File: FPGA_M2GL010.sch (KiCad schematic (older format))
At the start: 19 parts

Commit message: Does this actually work, Git?
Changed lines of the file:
@@
 Text Notes 5750 2700 0    50   ~ 10
 2.5V BANK!!
+Wire Wire Line
+	6150 5950 6150 6000
+Wire Wire Line
+	5550 5950 6150 5950
 $EndSCHEMATC

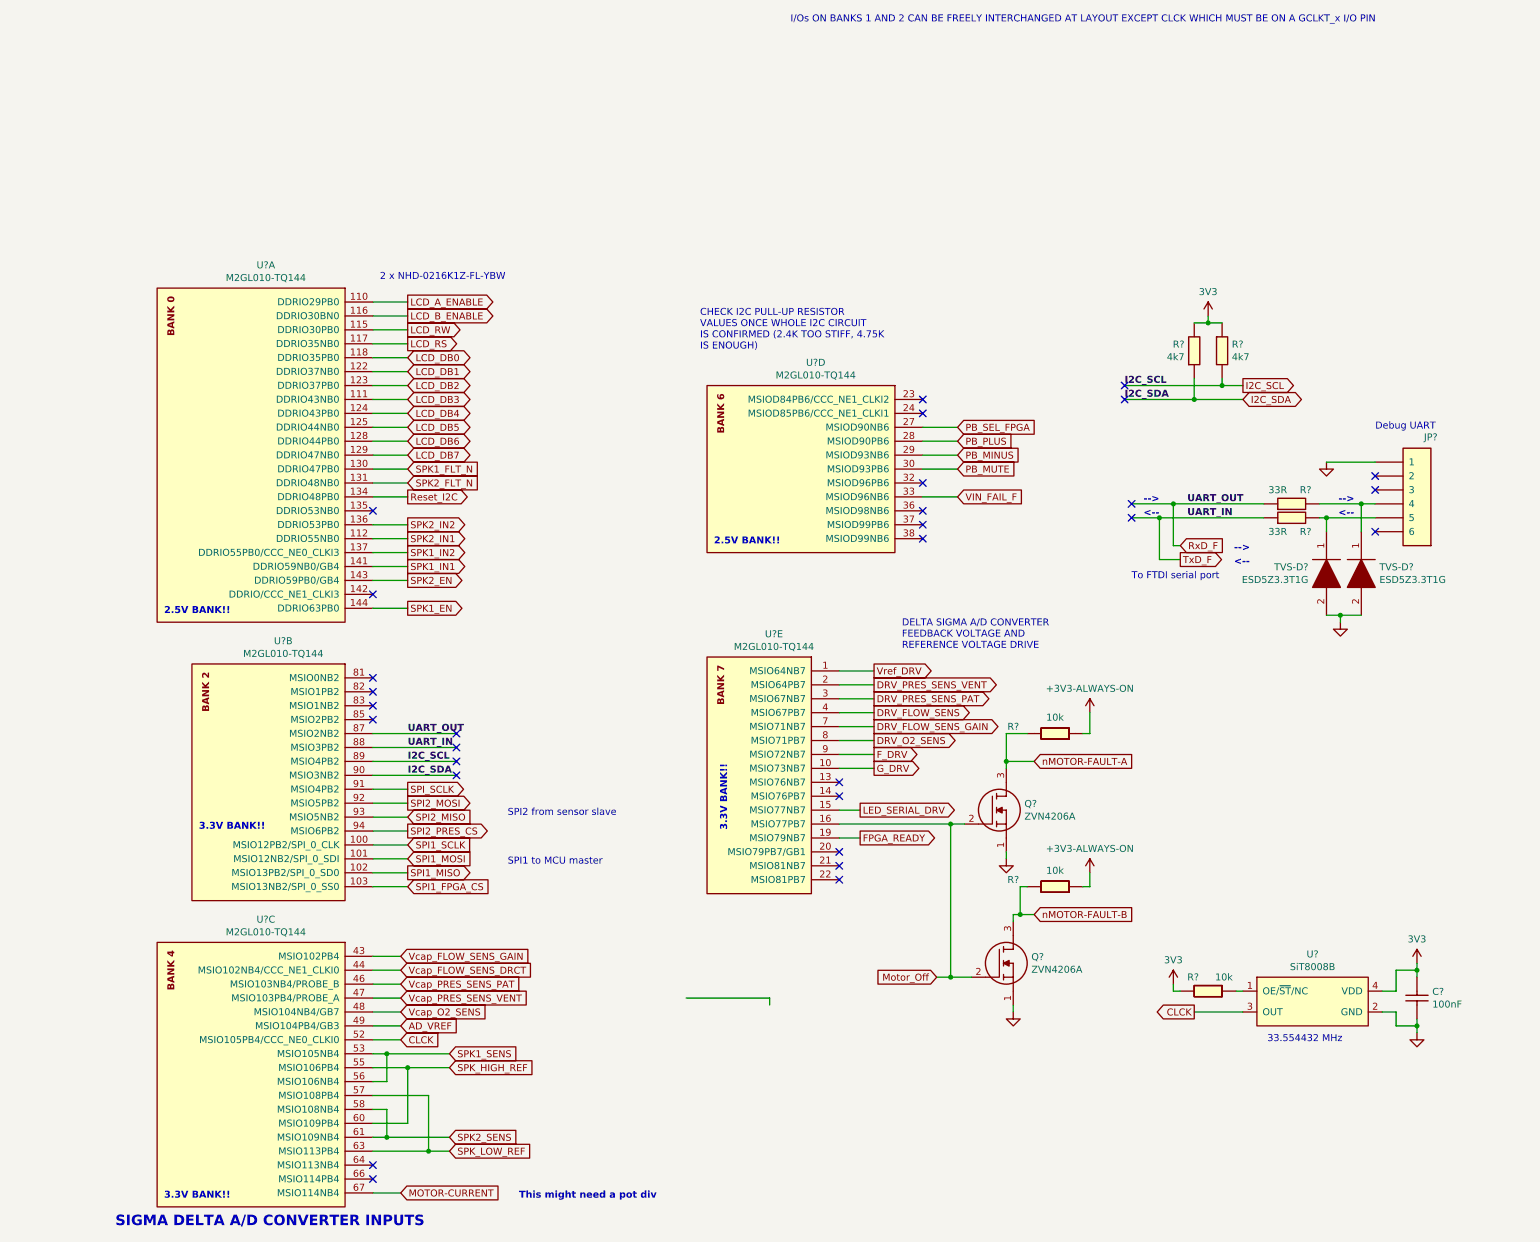
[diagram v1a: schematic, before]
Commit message: Finalised most of the schematic. I think there are a few more things to do in the Speaker
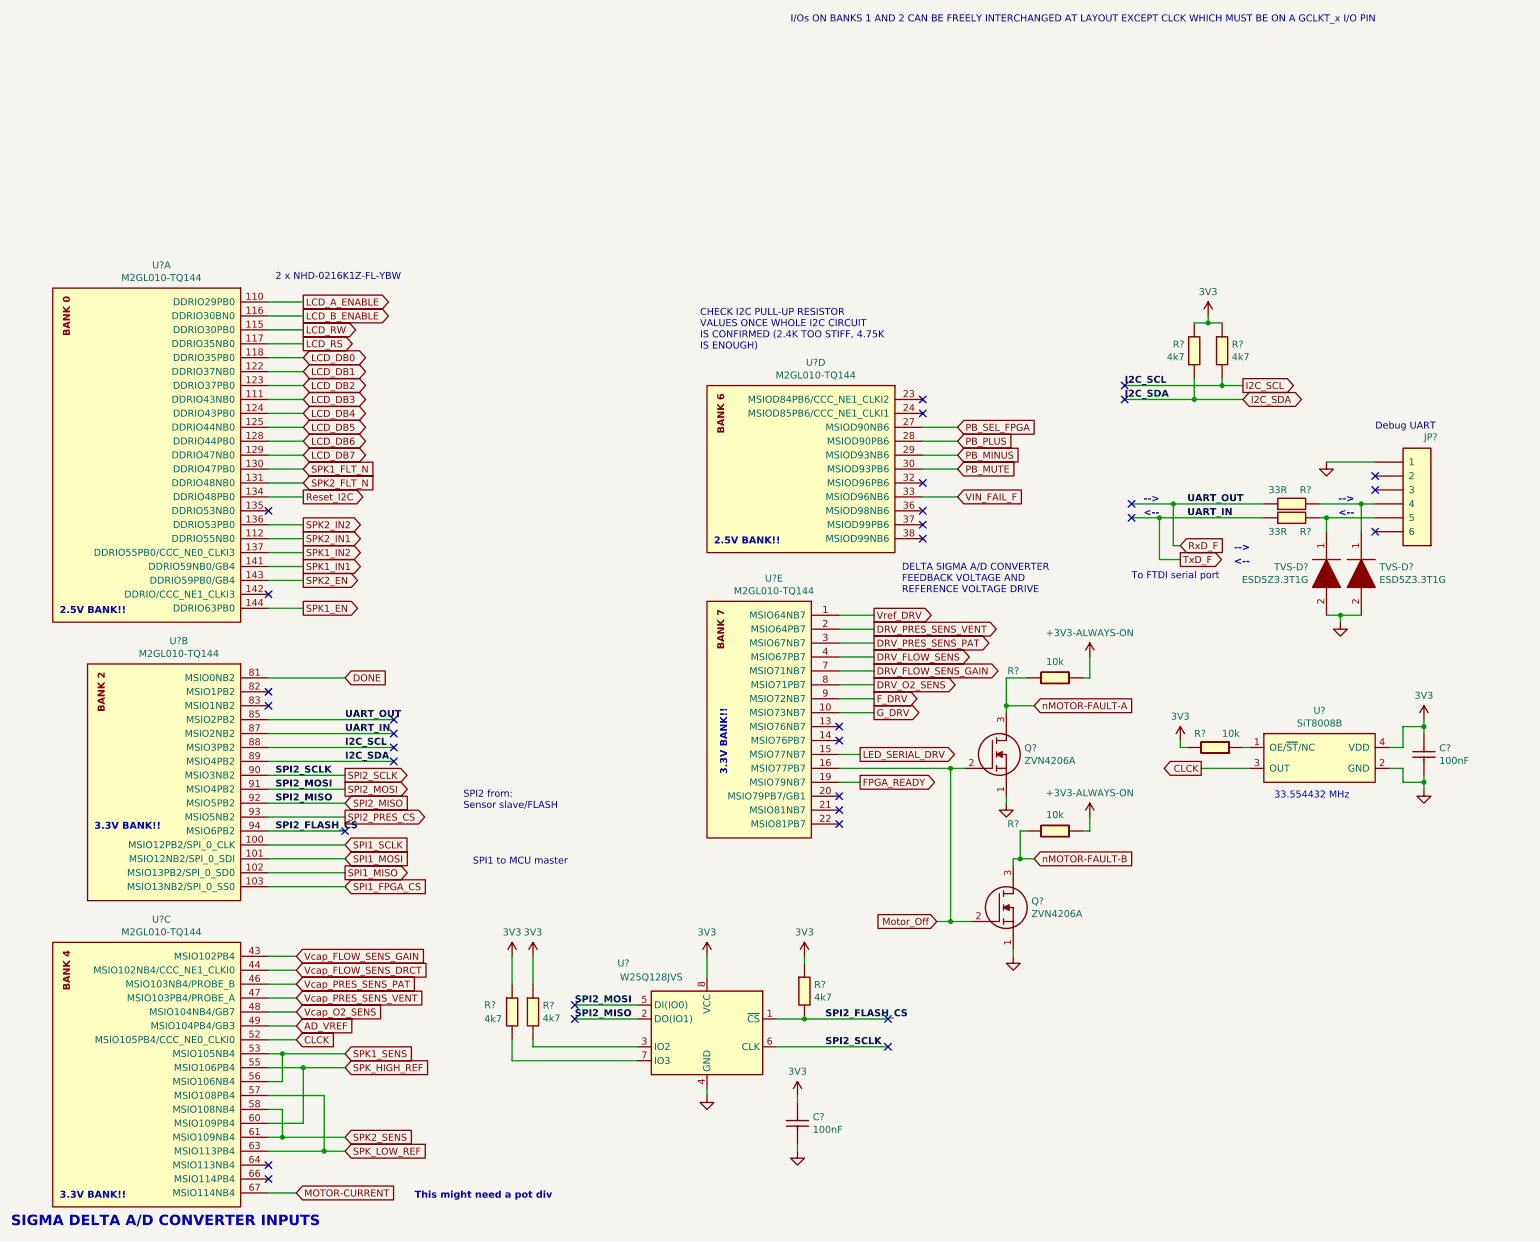
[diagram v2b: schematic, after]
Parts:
- added C?: 100nF_0603_Ceramic_Capacitor,_10%,_X7R,_25V, symbol OpenVent:100nF_0603_Ceramic_Capacitor,_10%,_X7R,_25V
- added R? (x3): 4.7K_±0.1%_1_6W_±25ppm_℃_0603_High_Precision_&_Lo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, symbol OpenVent:4.7K_±0.1%_1_6W_±25ppm_℃_0603_High_Precision_&_Low_TCR_SMD_Resistors_R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
- added U?: W25Q128JVS, Package_SO:SOIC-8_5.23x5.23mm_P1.27mm, symbol Memory_Flash:W25Q128JVS
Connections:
- net SPI_SCLK is gone; now on net SPI2_MOSI: U?.91 (MSIO4PB2)
- net +3V3: now also C?.1, R?.1, R?.1, R?.1, U?.8 (VCC)
- net GND: now also C?.2, U?.4 (GND)
- net I2C_SCL: now also U?.88 (MSIO3PB2); no longer U?.89 (MSIO4PB2)
- net I2C_SDA: now also U?.89 (MSIO4PB2); no longer U?.90 (MSIO3NB2)
- net RxD_F: now also U?.85 (MSIO2PB2); no longer U?.87 (MSIO2NB2)
- net SPI2_MISO: now also U?.92 (MSIO5PB2), U?.2 (DO(IO1)); no longer U?.93 (MSIO5NB2)
- net SPI2_MOSI: now also U?.5 (DI(IO0)); no longer U?.92 (MSIO5PB2)
- net SPI2_PRES_CS: now also U?.93 (MSIO5NB2); no longer U?.94 (MSIO6PB2)
- net TxD_F: now also U?.87 (MSIO2NB2); no longer U?.88 (MSIO3PB2)
- net DONE: now reaches U?.81 (MSIO0NB2)
- new net: R?.2, U?.3 (IO2)
- new net: R?.2, U?.7 (IO3)
- new net SPI2_FLASH_CS: R?.2, U?.1 (~CS), U?.94 (MSIO6PB2)
- new net SPI2_SCLK: U?.6 (CLK), U?.90 (MSIO3NB2)
- no-connect marks 30 -> 33
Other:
- note added: "SPI2 from: \nSensor slave/FLASH\n"
- note removed: "SPI2 from sensor slave"
- moved on the sheet: C?, Q?, R?, U?, U?A, U?B, U?C, U?E

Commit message: Finished assigning 2.5V signals, completed the Sigma Delta inputs, added FPGA testpoints
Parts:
- added TP? (x8): TestPoint, symbol Connector:TestPoint
- U?: symbol Memory_Flash:W25Q128JVS -> OpenVent-rescue:W25Q128JVS-Memory_Flash
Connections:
- net labels added: FPGA_TP_1, FPGA_TP_2, FPGA_TP_3, FPGA_TP_4, FPGA_TP_5, FPGA_TP_6, FPGA_TP_7, FPGA_TP_8
- wire segments 151 -> 167
- no-connect marks 33 -> 25
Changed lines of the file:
@@
 EESchema Schematic File Version 4
-EELAYER 30 0
+LIBS:OpenVent-cache
+EELAYER 26 0
 EELAYER END
 $Descr A4 11693 8268
@@
 Connection ~ 2950 7050
 Connection ~ 2650 6950
-Text GLabel 7500 2350 2    50   Input ~ 0
+Text GLabel 2800 2450 2    50   Input ~ 0
 VIN_FAIL_F
 Wire Wire Line
@@
 Text GLabel 2750 6250 2    50   Input ~ 0
 CLCK
-Wire Wire Line
-	7250 1850 7500 1850
-Text GLabel 7500 1850 2    50   Input ~ 0
+Text GLabel 6750 4700 2    50   Input ~ 0
 PB_SEL_FPGA
-NoConn ~ 2550 2450
-Text GLabel 7500 2050 2    50   Input ~ 0
+Text GLabel 7900 1750 2    50   Input ~ 0
 PB_MINUS
-Text GLabel 7500 1950 2    50   Input ~ 0
+Text GLabel 7900 1650 2    50   Input ~ 0
 PB_PLUS
-Text GLabel 7500 2150 2    50   Input ~ 0
+Text GLabel 7900 1850 2    50   Input ~ 0
 PB_MUTE
-Wire Wire Line
-	7500 2150 7250 2150
-Wire Wire Line
-	7250 2050 7500 2050
-Wire Wire Line
-	7250 1950 7500 1950
 Wire Wire Line
 	2750 6250 2550 6250
@@
 NoConn ~ 2550 7250
 Wire Wire Line
-	7500 2350 7250 2350
-NoConn ~ 7250 2250
-NoConn ~ 7250 2450
-NoConn ~ 7250 2550
-NoConn ~ 7250 2650
+	2800 2450 2550 2450
 Text GLabel 9550 1550 2    50   Output ~ 0
 I2C_SCL
@@
 NoConn ~ 6650 4500
 NoConn ~ 6650 4600
-NoConn ~ 6650 4700
-NoConn ~ 7250 1650
-NoConn ~ 7250 1750
 Wire Wire Line
 	2750 7350 2550 7350
@@
 SPI2_MOSI
 $Comp
-L Memory_Flash:W25Q128JVS U?
+L OpenVent-rescue:W25Q128JVS-Memory_Flash U?
 U 1 1 61F50A78
 P 5700 6200
@@
 Wire Wire Line
 	6350 6650 6350 6700
+Wire Wire Line
+	6750 4700 6650 4700
+Text Label 7400 1950 0    50   ~ 10
+FPGA_TP_1
+Wire Wire Line
+	7250 1850 7900 1850
+Wire Wire Line
+	7250 1750 7900 1750
+Wire Wire Line
+	7250 1650 7900 1650
+Text Label 7400 2050 0    50   ~ 10
+FPGA_TP_2
+Text Label 7400 2150 0    50   ~ 10
+FPGA_TP_3
+Text Label 7400 2250 0    50   ~ 10
+FPGA_TP_4
+Text Label 7400 2350 0    50   ~ 10
+FPGA_TP_5
+Text Label 7400 2450 0    50   ~ 10
+FPGA_TP_6
+Text Label 7400 2550 0    50   ~ 10
+FPGA_TP_7
+Text Label 7400 2650 0    50   ~ 10
+FPGA_TP_8
+Wire Wire Line
+	7400 2650 7250 2650
+Wire Wire Line
+	7250 2550 7400 2550
+Wire Wire Line
+	7400 2450 7250 2450
+Wire Wire Line
+	7250 2350 7400 2350
+Wire Wire Line
+	7400 2250 7250 2250
+Wire Wire Line
+	7250 2150 7400 2150
+Wire Wire Line
+	7400 2050 7250 2050
+Wire Wire Line
+	7250 1950 7400 1950
+$Comp
+L Connector:TestPoint TP?
+U 1 1 623FA0A6
+P 9900 5150
+F 0 "TP?" V 9900 5338 50  0000 L CNN
+F 1 "TestPoint" V 9945 5338 50  0001 L CNN
+F 2 "" H 10100 5150 50  0001 C CNN
+F 3 "~" H 10100 5150 50  0001 C CNN
+	1    9900 5150
+	0    1    1    0
+$EndComp
+$Comp
+L Connector:TestPoint TP?
+U 1 1 62415585
+P 9900 5050
+F 0 "TP?" V 9900 5238 50  0000 L CNN
+F 1 "TestPoint" V 9945 5238 50  0001 L CNN
+F 2 "" H 10100 5050 50  0001 C CNN
+F 3 "~" H 10100 5050 50  0001 C CNN
+	1    9900 5050
+	0    1    1    0
+$EndComp
+$Comp
+L Connector:TestPoint TP?
+U 1 1 624155CD
+P 9900 5250
+F 0 "TP?" V 9900 5438 50  0000 L CNN
+F 1 "TestPoint" V 9945 5438 50  0001 L CNN
+F 2 "" H 10100 5250 50  0001 C CNN
+F 3 "~" H 10100 5250 50  0001 C CNN
+	1    9900 5250
+	0    1    1    0
+$EndComp
+$Comp
+L Connector:TestPoint TP?
+U 1 1 62415617
+P 9900 5350
+F 0 "TP?" V 9900 5538 50  0000 L CNN
+F 1 "TestPoint" V 9945 5538 50  0001 L CNN
+F 2 "" H 10100 5350 50  0001 C CNN
+F 3 "~" H 10100 5350 50  0001 C CNN
+	1    9900 5350
+	0    1    1    0
+$EndComp
+$Comp
+L Connector:TestPoint TP?
+U 1 1 6241565F
+P 9900 5450
+F 0 "TP?" V 9900 5638 50  0000 L CNN
+F 1 "TestPoint" V 9945 5638 50  0001 L CNN
+F 2 "" H 10100 5450 50  0001 C CNN
+F 3 "~" H 10100 5450 50  0001 C CNN
+	1    9900 5450
+	0    1    1    0
+$EndComp
+$Comp
+L Connector:TestPoint TP?
+U 1 1 624156A9
+P 9900 5550
+F 0 "TP?" V 9900 5738 50  0000 L CNN
+F 1 "TestPoint" V 9945 5738 50  0001 L CNN
+F 2 "" H 10100 5550 50  0001 C CNN
+F 3 "~" H 10100 5550 50  0001 C CNN
+	1    9900 5550
+	0    1    1    0
+$EndComp
+$Comp
+L Connector:TestPoint TP?
+U 1 1 624156F5
+P 9900 5650
+F 0 "TP?" V 9900 5838 50  0000 L CNN
+F 1 "TestPoint" V 9945 5838 50  0001 L CNN
+F 2 "" H 10100 5650 50  0001 C CNN
+F 3 "~" H 10100 5650 50  0001 C CNN
+	1    9900 5650
+	0    1    1    0
+$EndComp
+$Comp
+L Connector:TestPoint TP?
+U 1 1 62415743
+P 9900 5750
+F 0 "TP?" V 9900 5938 50  0000 L CNN
+F 1 "TestPoint" V 9945 5938 50  0001 L CNN
+F 2 "" H 10100 5750 50  0001 C CNN
+F 3 "~" H 10100 5750 50  0001 C CNN
+	1    9900 5750
+	0    1    1    0
+$EndComp
+Text Label 9400 5050 0    50   ~ 10
+FPGA_TP_1
+Text Label 9400 5150 0    50   ~ 10
+FPGA_TP_2
+Text Label 9400 5250 0    50   ~ 10
+FPGA_TP_3
+Text Label 9400 5350 0    50   ~ 10
+FPGA_TP_4
+Text Label 9400 5450 0    50   ~ 10
+FPGA_TP_5
+Text Label 9400 5550 0    50   ~ 10
+FPGA_TP_6
+Text Label 9400 5650 0    50   ~ 10
+FPGA_TP_7
+Text Label 9400 5750 0    50   ~ 10
+FPGA_TP_8
+Wire Wire Line
+	9900 5050 9400 5050
+Wire Wire Line
+	9400 5150 9900 5150
+Wire Wire Line
+	9900 5250 9400 5250
+Wire Wire Line
+	9400 5350 9900 5350
+Wire Wire Line
+	9900 5450 9400 5450
+Wire Wire Line
+	9400 5550 9900 5550
+Wire Wire Line
+	9900 5650 9400 5650
+Wire Wire Line
+	9450 5750 9900 5750
 $EndSCHEMATC
